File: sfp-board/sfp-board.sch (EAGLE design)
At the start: 22 parts

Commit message: board v18
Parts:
- R4: device rcl:R-US_0411/15 -> rcl:R-US_0411/3V
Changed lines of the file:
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@@
 <grid distance="0.1" unitdist="inch" unit="inch" style="lines" multiple="1" display="no" altdistance="0.01" altunitdist="inch" altunit="inch"/>
 <layers>
-<layer number="1" name="Top" color="4" fill="1" visible="no" active="no"/>
-<layer number="2" name="Route2" color="1" fill="3" visible="no" active="no"/>
-<layer number="3" name="Route3" color="4" fill="3" visible="no" active="no"/>
-<layer number="4" name="Route4" color="1" fill="4" visible="no" active="no"/>
-<layer number="5" name="Route5" color="4" fill="4" visible="no" active="no"/>
-<layer number="6" name="Route6" color="1" fill="8" visible="no" active="no"/>
-<layer number="7" name="Route7" color="4" fill="8" visible="no" active="no"/>
-<layer number="8" name="Route8" color="1" fill="2" visible="no" active="no"/>
-<layer number="9" name="Route9" color="4" fill="2" visible="no" active="no"/>
-<layer number="10" name="Route10" color="1" fill="7" visible="no" active="no"/>
-<layer number="11" name="Route11" color="4" fill="7" visible="no" active="no"/>
-<layer number="12" name="Route12" color="1" fill="5" visible="no" active="no"/>
-<layer number="13" name="Route13" color="4" fill="5" visible="no" active="no"/>
-<layer number="14" name="Route14" color="1" fill="6" visible="no" active="no"/>
-<layer number="15" name="Route15" color="4" fill="6" visible="no" active="no"/>
-<layer number="16" name="Bottom" color="1" fill="1" visible="no" active="no"/>
-<layer number="17" name="Pads" color="2" fill="1" visible="no" active="no"/>
-<layer number="18" name="Vias" color="2" fill="1" visible="no" active="no"/>
-<layer number="19" name="Unrouted" color="6" fill="1" visible="no" active="no"/>
-<layer number="20" name="Dimension" color="15" fill="1" visible="no" active="no"/>
-<layer number="21" name="tPlace" color="7" fill="1" visible="no" active="no"/>
-<layer number="22" name="bPlace" color="7" fill="1" visible="no" active="no"/>
-<layer number="23" name="tOrigins" color="15" fill="1" visible="no" active="no"/>
-<layer number="24" name="bOrigins" color="15" fill="1" visible="no" active="no"/>
-<layer number="25" name="tNames" color="7" fill="1" visible="no" active="no"/>
-<layer number="26" name="bNames" color="7" fill="1" visible="no" active="no"/>
-<layer number="27" name="tValues" color="7" fill="1" visible="no" active="no"/>
-<layer number="28" name="bValues" color="7" fill="1" visible="no" active="no"/>
+<layer number="1" name="Top" color="4" fill="1" visible="yes" active="no"/>
+<layer number="2" name="Route2" color="1" fill="3" visible="yes" active="no"/>
+<layer number="3" name="Route3" color="4" fill="3" visible="yes" active="no"/>
+<layer number="4" name="Route4" color="1" fill="4" visible="yes" active="no"/>
+<layer number="5" name="Route5" color="4" fill="4" visible="yes" active="no"/>
+<layer number="6" name="Route6" color="1" fill="8" visible="yes" active="no"/>
+<layer number="7" name="Route7" color="4" fill="8" visible="yes" active="no"/>
+<layer number="8" name="Route8" color="1" fill="2" visible="yes" active="no"/>
+<layer number="9" name="Route9" color="4" fill="2" visible="yes" active="no"/>
+<layer number="10" name="Route10" color="1" fill="7" visible="yes" active="no"/>
+<layer number="11" name="Route11" color="4" fill="7" visible="yes" active="no"/>
+<layer number="12" name="Route12" color="1" fill="5" visible="yes" active="no"/>
+<layer number="13" name="Route13" color="4" fill="5" visible="yes" active="no"/>
+<layer number="14" name="Route14" color="1" fill="6" visible="yes" active="no"/>
+<layer number="15" name="Route15" color="4" fill="6" visible="yes" active="no"/>
+<layer number="16" name="Bottom" color="1" fill="1" visible="yes" active="no"/>
+<layer number="17" name="Pads" color="2" fill="1" visible="yes" active="no"/>
+<layer number="18" name="Vias" color="2" fill="1" visible="yes" active="no"/>
+<layer number="19" name="Unrouted" color="6" fill="1" visible="yes" active="no"/>
+<layer number="20" name="Dimension" color="15" fill="1" visible="yes" active="no"/>
+<layer number="21" name="tPlace" color="7" fill="1" visible="yes" active="no"/>
+<layer number="22" name="bPlace" color="7" fill="1" visible="yes" active="no"/>
+<layer number="23" name="tOrigins" color="15" fill="1" visible="yes" active="no"/>
+<layer number="24" name="bOrigins" color="15" fill="1" visible="yes" active="no"/>
+<layer number="25" name="tNames" color="7" fill="1" visible="yes" active="no"/>
+<layer number="26" name="bNames" color="7" fill="1" visible="yes" active="no"/>
+<layer number="27" name="tValues" color="7" fill="1" visible="yes" active="no"/>
+<layer number="28" name="bValues" color="7" fill="1" visible="yes" active="no"/>
 <layer number="29" name="tStop" color="7" fill="3" visible="no" active="no"/>
 <layer number="30" name="bStop" color="7" fill="6" visible="no" active="no"/>
@@
 <layer number="35" name="tGlue" color="7" fill="4" visible="no" active="no"/>
 <layer number="36" name="bGlue" color="7" fill="5" visible="no" active="no"/>
-<layer number="37" name="tTest" color="7" fill="1" visible="no" active="no"/>
-<layer number="38" name="bTest" color="7" fill="1" visible="no" active="no"/>
+<layer number="37" name="tTest" color="7" fill="1" visible="yes" active="no"/>
+<layer number="38" name="bTest" color="7" fill="1" visible="yes" active="no"/>
 <layer number="39" name="tKeepout" color="4" fill="11" visible="no" active="no"/>
 <layer number="40" name="bKeepout" color="1" fill="11" visible="no" active="no"/>
@@
 <layer number="44" name="Drills" color="7" fill="1" visible="no" active="no"/>
 <layer number="45" name="Holes" color="7" fill="1" visible="no" active="no"/>
-<layer number="46" name="Milling" color="3" fill="1" visible="no" active="no"/>
-<layer number="47" name="Measures" color="7" fill="1" visible="no" active="no"/>
-<layer number="48" name="Document" color="7" fill="1" visible="no" active="no"/>
-<layer number="49" name="Reference" color="7" fill="1" visible="no" active="no"/>
-<layer number="50" name="dxf" color="7" fill="1" visible="no" active="no"/>
-<layer number="51" name="tDocu" color="7" fill="1" visible="no" active="no"/>
-<layer number="52" name="bDocu" color="7" fill="1" visible="no" active="no"/>
-<layer number="53" name="tGND_GNDA" color="7" fill="9" visible="no" active="no"/>
-<layer number="54" name="bGND_GNDA" color="1" fill="9" visible="no" active="no"/>
-<layer number="56" name="wert" color="7" fill="1" visible="no" active="no"/>
-<layer number="57" name="tCAD" color="7" fill="1" visible="no" active="no"/>
-<layer number="59" name="tCarbon" color="7" fill="1" visible="no" active="no"/>
-<layer number="60" name="bCarbon" color="7" fill="1" visible="no" active="no"/>
+<layer number="46" name="Milling" color="3" fill="1" visible="yes" active="no"/>
+<layer number="47" name="Measures" color="7" fill="1" visible="yes" active="no"/>
+<layer number="48" name="Document" color="7" fill="1" visible="yes" active="no"/>
+<layer number="49" name="Reference" color="7" fill="1" visible="yes" active="no"/>
+<layer number="50" name="dxf" color="7" fill="1" visible="yes" active="no"/>
+<layer number="51" name="tDocu" color="7" fill="1" visible="yes" active="no"/>
+<layer number="52" name="bDocu" color="7" fill="1" visible="yes" active="no"/>
+<layer number="53" name="tGND_GNDA" color="7" fill="9" visible="yes" active="no"/>
+<layer number="54" name="bGND_GNDA" color="1" fill="9" visible="yes" active="no"/>
+<layer number="56" name="wert" color="7" fill="1" visible="yes" active="no"/>
+<layer number="57" name="tCAD" color="7" fill="1" visible="yes" active="no"/>
+<layer number="59" name="tCarbon" color="7" fill="1" visible="yes" active="no"/>
+<layer number="60" name="bCarbon" color="7" fill="1" visible="yes" active="no"/>
 <layer number="88" name="SimResults" color="9" fill="1" visible="yes" active="yes"/>
 <layer number="89" name="SimProbes" color="9" fill="1" visible="yes" active="yes"/>
@@
 <part name="H3" library="holes" deviceset="MOUNT-HOLE" device="3.3"/>
 <part name="H4" library="holes" deviceset="MOUNT-HOLE" device="3.3"/>
-<part name="R4" library="rcl" deviceset="R-US_" device="0411/15" value="Photoresistor"/>
+<part name="R4" library="rcl" deviceset="R-US_" device="0411/3V" value="Photoresistor"/>
 <part name="LED1" library="adafruit" deviceset="LED" device="5MM" value="status 2"/>
 <part name="LED2" library="adafruit" deviceset="LED" device="5MM" value="power"/>

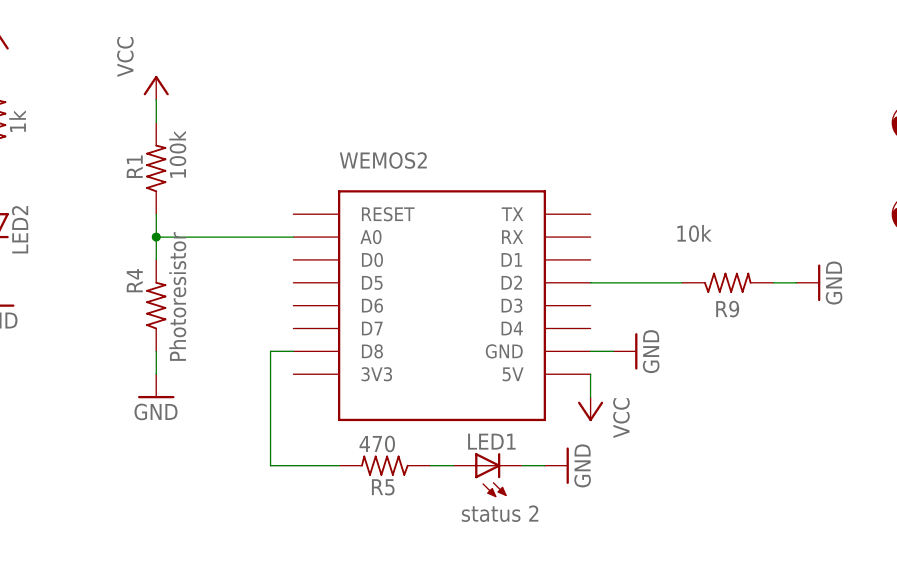
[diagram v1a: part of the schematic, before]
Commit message: Final board arrangement
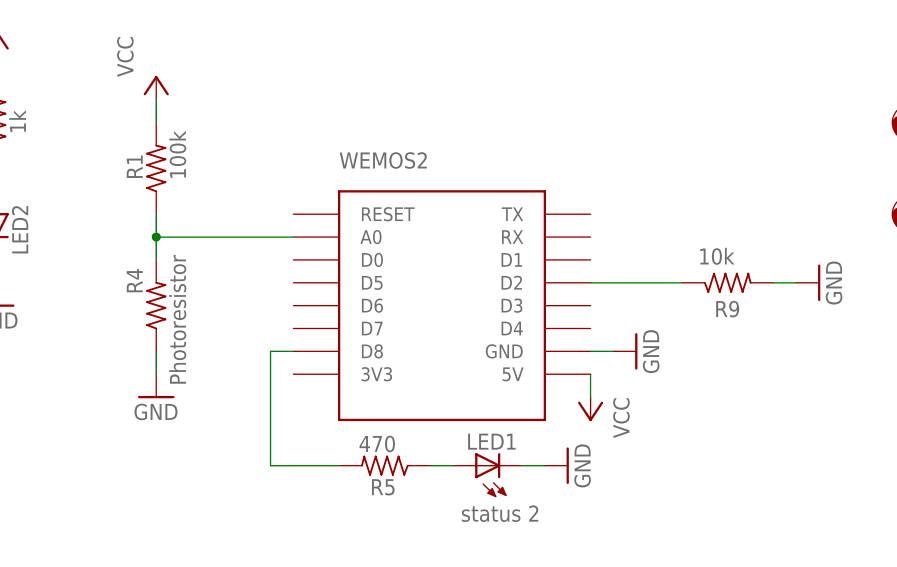
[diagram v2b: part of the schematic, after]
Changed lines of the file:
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@@
 <grid distance="0.1" unitdist="inch" unit="inch" style="lines" multiple="1" display="no" altdistance="0.01" altunitdist="inch" altunit="inch"/>
 <layers>
-<layer number="1" name="Top" color="4" fill="1" visible="yes" active="no"/>
-<layer number="2" name="Route2" color="1" fill="3" visible="yes" active="no"/>
-<layer number="3" name="Route3" color="4" fill="3" visible="yes" active="no"/>
-<layer number="4" name="Route4" color="1" fill="4" visible="yes" active="no"/>
-<layer number="5" name="Route5" color="4" fill="4" visible="yes" active="no"/>
-<layer number="6" name="Route6" color="1" fill="8" visible="yes" active="no"/>
-<layer number="7" name="Route7" color="4" fill="8" visible="yes" active="no"/>
-<layer number="8" name="Route8" color="1" fill="2" visible="yes" active="no"/>
-<layer number="9" name="Route9" color="4" fill="2" visible="yes" active="no"/>
-<layer number="10" name="Route10" color="1" fill="7" visible="yes" active="no"/>
-<layer number="11" name="Route11" color="4" fill="7" visible="yes" active="no"/>
-<layer number="12" name="Route12" color="1" fill="5" visible="yes" active="no"/>
-<layer number="13" name="Route13" color="4" fill="5" visible="yes" active="no"/>
-<layer number="14" name="Route14" color="1" fill="6" visible="yes" active="no"/>
-<layer number="15" name="Route15" color="4" fill="6" visible="yes" active="no"/>
-<layer number="16" name="Bottom" color="1" fill="1" visible="yes" active="no"/>
-<layer number="17" name="Pads" color="2" fill="1" visible="yes" active="no"/>
-<layer number="18" name="Vias" color="2" fill="1" visible="yes" active="no"/>
-<layer number="19" name="Unrouted" color="6" fill="1" visible="yes" active="no"/>
-<layer number="20" name="Dimension" color="15" fill="1" visible="yes" active="no"/>
-<layer number="21" name="tPlace" color="7" fill="1" visible="yes" active="no"/>
-<layer number="22" name="bPlace" color="7" fill="1" visible="yes" active="no"/>
-<layer number="23" name="tOrigins" color="15" fill="1" visible="yes" active="no"/>
-<layer number="24" name="bOrigins" color="15" fill="1" visible="yes" active="no"/>
-<layer number="25" name="tNames" color="7" fill="1" visible="yes" active="no"/>
-<layer number="26" name="bNames" color="7" fill="1" visible="yes" active="no"/>
-<layer number="27" name="tValues" color="7" fill="1" visible="yes" active="no"/>
-<layer number="28" name="bValues" color="7" fill="1" visible="yes" active="no"/>
+<layer number="1" name="Top" color="4" fill="1" visible="no" active="no"/>
+<layer number="2" name="Route2" color="1" fill="3" visible="no" active="no"/>
+<layer number="3" name="Route3" color="4" fill="3" visible="no" active="no"/>
+<layer number="4" name="Route4" color="1" fill="4" visible="no" active="no"/>
+<layer number="5" name="Route5" color="4" fill="4" visible="no" active="no"/>
+<layer number="6" name="Route6" color="1" fill="8" visible="no" active="no"/>
+<layer number="7" name="Route7" color="4" fill="8" visible="no" active="no"/>
+<layer number="8" name="Route8" color="1" fill="2" visible="no" active="no"/>
+<layer number="9" name="Route9" color="4" fill="2" visible="no" active="no"/>
+<layer number="10" name="Route10" color="1" fill="7" visible="no" active="no"/>
+<layer number="11" name="Route11" color="4" fill="7" visible="no" active="no"/>
+<layer number="12" name="Route12" color="1" fill="5" visible="no" active="no"/>
+<layer number="13" name="Route13" color="4" fill="5" visible="no" active="no"/>
+<layer number="14" name="Route14" color="1" fill="6" visible="no" active="no"/>
+<layer number="15" name="Route15" color="4" fill="6" visible="no" active="no"/>
+<layer number="16" name="Bottom" color="1" fill="1" visible="no" active="no"/>
+<layer number="17" name="Pads" color="2" fill="1" visible="no" active="no"/>
+<layer number="18" name="Vias" color="2" fill="1" visible="no" active="no"/>
+<layer number="19" name="Unrouted" color="6" fill="1" visible="no" active="no"/>
+<layer number="20" name="Dimension" color="15" fill="1" visible="no" active="no"/>
+<layer number="21" name="tPlace" color="7" fill="1" visible="no" active="no"/>
+<layer number="22" name="bPlace" color="7" fill="1" visible="no" active="no"/>
+<layer number="23" name="tOrigins" color="15" fill="1" visible="no" active="no"/>
+<layer number="24" name="bOrigins" color="15" fill="1" visible="no" active="no"/>
+<layer number="25" name="tNames" color="7" fill="1" visible="no" active="no"/>
+<layer number="26" name="bNames" color="7" fill="1" visible="no" active="no"/>
+<layer number="27" name="tValues" color="7" fill="1" visible="no" active="no"/>
+<layer number="28" name="bValues" color="7" fill="1" visible="no" active="no"/>
 <layer number="29" name="tStop" color="7" fill="3" visible="no" active="no"/>
 <layer number="30" name="bStop" color="7" fill="6" visible="no" active="no"/>
@@
 <layer number="35" name="tGlue" color="7" fill="4" visible="no" active="no"/>
 <layer number="36" name="bGlue" color="7" fill="5" visible="no" active="no"/>
-<layer number="37" name="tTest" color="7" fill="1" visible="yes" active="no"/>
-<layer number="38" name="bTest" color="7" fill="1" visible="yes" active="no"/>
+<layer number="37" name="tTest" color="7" fill="1" visible="no" active="no"/>
+<layer number="38" name="bTest" color="7" fill="1" visible="no" active="no"/>
 <layer number="39" name="tKeepout" color="4" fill="11" visible="no" active="no"/>
 <layer number="40" name="bKeepout" color="1" fill="11" visible="no" active="no"/>
@@
 <layer number="44" name="Drills" color="7" fill="1" visible="no" active="no"/>
 <layer number="45" name="Holes" color="7" fill="1" visible="no" active="no"/>
-<layer number="46" name="Milling" color="3" fill="1" visible="yes" active="no"/>
-<layer number="47" name="Measures" color="7" fill="1" visible="yes" active="no"/>
-<layer number="48" name="Document" color="7" fill="1" visible="yes" active="no"/>
-<layer number="49" name="Reference" color="7" fill="1" visible="yes" active="no"/>
-<layer number="50" name="dxf" color="7" fill="1" visible="yes" active="no"/>
-<layer number="51" name="tDocu" color="7" fill="1" visible="yes" active="no"/>
-<layer number="52" name="bDocu" color="7" fill="1" visible="yes" active="no"/>
-<layer number="53" name="tGND_GNDA" color="7" fill="9" visible="yes" active="no"/>
-<layer number="54" name="bGND_GNDA" color="1" fill="9" visible="yes" active="no"/>
-<layer number="56" name="wert" color="7" fill="1" visible="yes" active="no"/>
-<layer number="57" name="tCAD" color="7" fill="1" visible="yes" active="no"/>
-<layer number="59" name="tCarbon" color="7" fill="1" visible="yes" active="no"/>
-<layer number="60" name="bCarbon" color="7" fill="1" visible="yes" active="no"/>
+<layer number="46" name="Milling" color="3" fill="1" visible="no" active="no"/>
+<layer number="47" name="Measures" color="7" fill="1" visible="no" active="no"/>
+<layer number="48" name="Document" color="7" fill="1" visible="no" active="no"/>
+<layer number="49" name="Reference" color="7" fill="1" visible="no" active="no"/>
+<layer number="50" name="dxf" color="7" fill="1" visible="no" active="no"/>
+<layer number="51" name="tDocu" color="7" fill="1" visible="no" active="no"/>
+<layer number="52" name="bDocu" color="7" fill="1" visible="no" active="no"/>
+<layer number="53" name="tGND_GNDA" color="7" fill="9" visible="no" active="no"/>
+<layer number="54" name="bGND_GNDA" color="1" fill="9" visible="no" active="no"/>
+<layer number="56" name="wert" color="7" fill="1" visible="no" active="no"/>
+<layer number="57" name="tCAD" color="7" fill="1" visible="no" active="no"/>
+<layer number="59" name="tCarbon" color="7" fill="1" visible="no" active="no"/>
+<layer number="60" name="bCarbon" color="7" fill="1" visible="no" active="no"/>
 <layer number="88" name="SimResults" color="9" fill="1" visible="yes" active="yes"/>
 <layer number="89" name="SimProbes" color="9" fill="1" visible="yes" active="yes"/>
@@
 <instance part="R4" gate="G$1" x="-27.94" y="86.36" smashed="yes" rot="R90">
 <attribute name="NAME" x="-29.4386" y="87.63" size="1.778" layer="95" rot="R90"/>
-<attribute name="VALUE" x="-24.638" y="80.01" size="1.778" layer="96" rot="R90"/>
+<attribute name="VALUE" x="-24.638" y="77.47" size="1.778" layer="96" rot="R90"/>
 </instance>
 <instance part="LED1" gate="G$1" x="7.62" y="68.58" smashed="yes" rot="R90">
@@
 <instance part="R9" gate="G$1" x="35.56" y="88.9" smashed="yes" rot="MR180">
 <attribute name="NAME" x="34.0614" y="85.09" size="1.778" layer="95"/>
-<attribute name="VALUE" x="33.782" y="95.25" size="1.778" layer="96" rot="R180"/>
+<attribute name="VALUE" x="36.322" y="92.71" size="1.778" layer="96" rot="R180"/>
 </instance>
 <instance part="P+8" gate="VCC" x="60.96" y="7.62" smashed="yes" rot="R270">

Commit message: Final Board arrangement #4
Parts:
- LED1, LED2, LED3: device adafruit:LED5MM -> digital-toy:LED5MM
- R1, R2, R3, R5, R6, R7, R9: device rcl:R-US_0411/15 -> digital-toy:RESISTOR0414/15
- R4: device rcl:R-US_0411/3V -> digital-toy:RESISTOR0414V
